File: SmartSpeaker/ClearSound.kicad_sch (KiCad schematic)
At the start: 51 parts

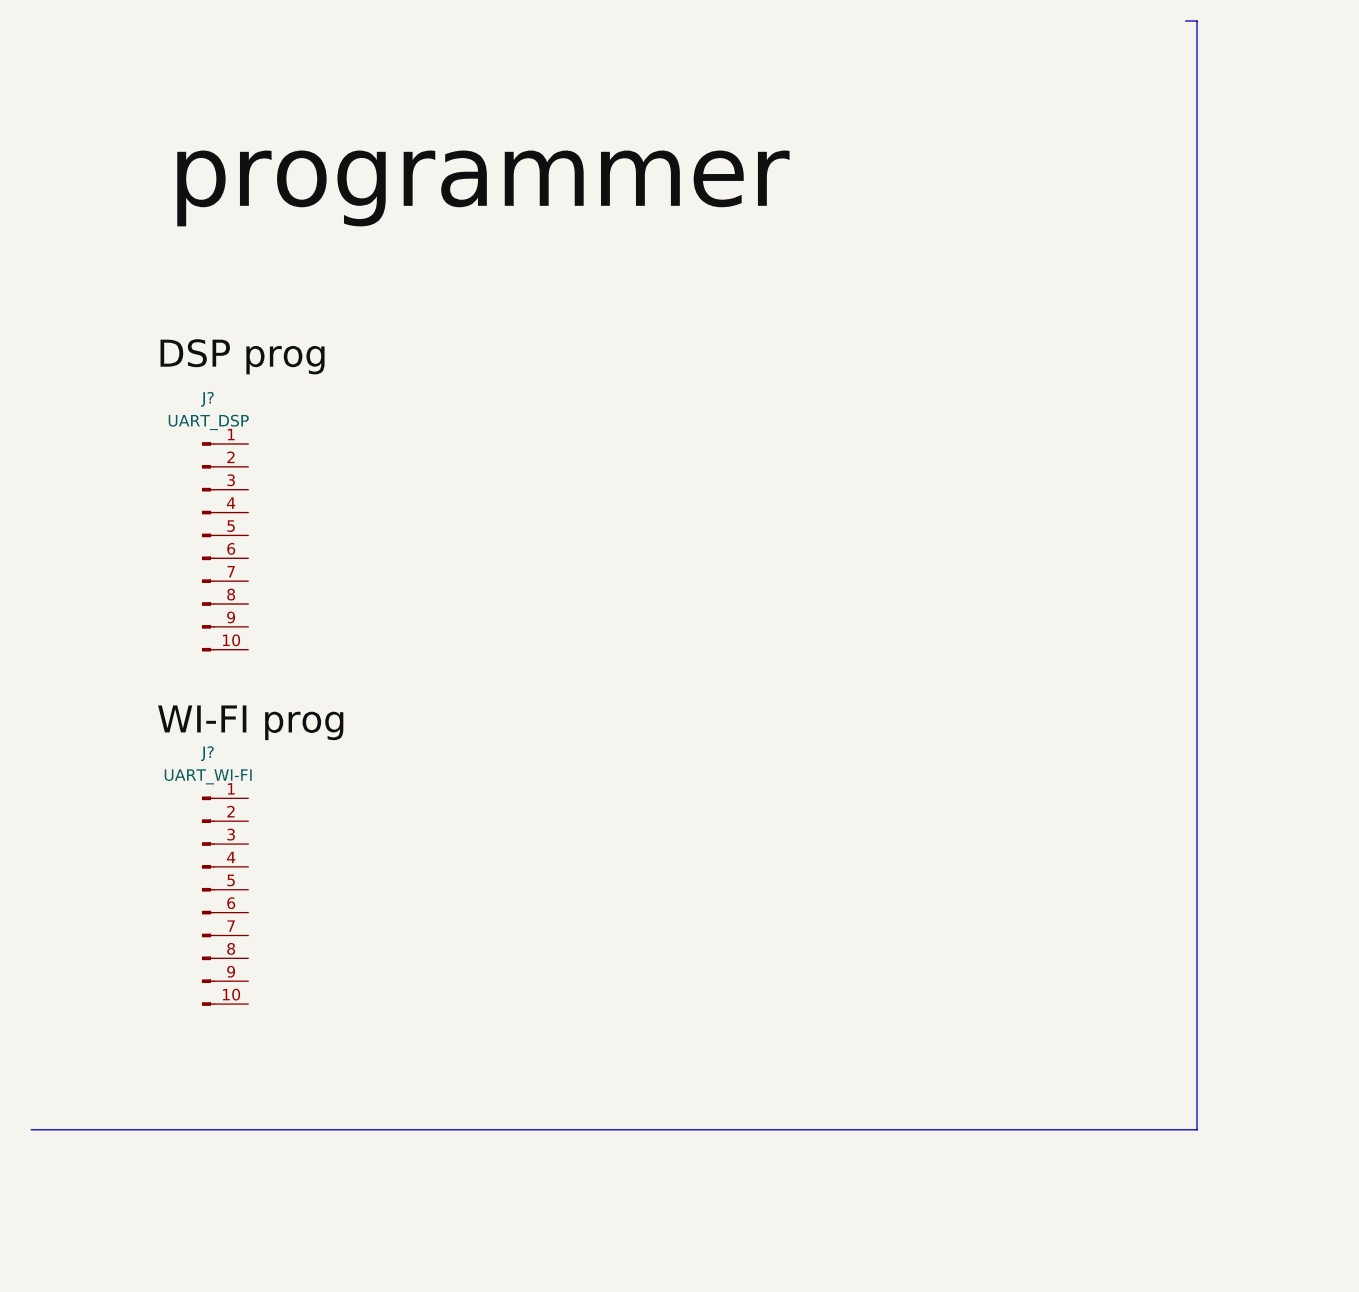
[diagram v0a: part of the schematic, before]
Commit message: UART header VDD/GND and interconnect now actually saved
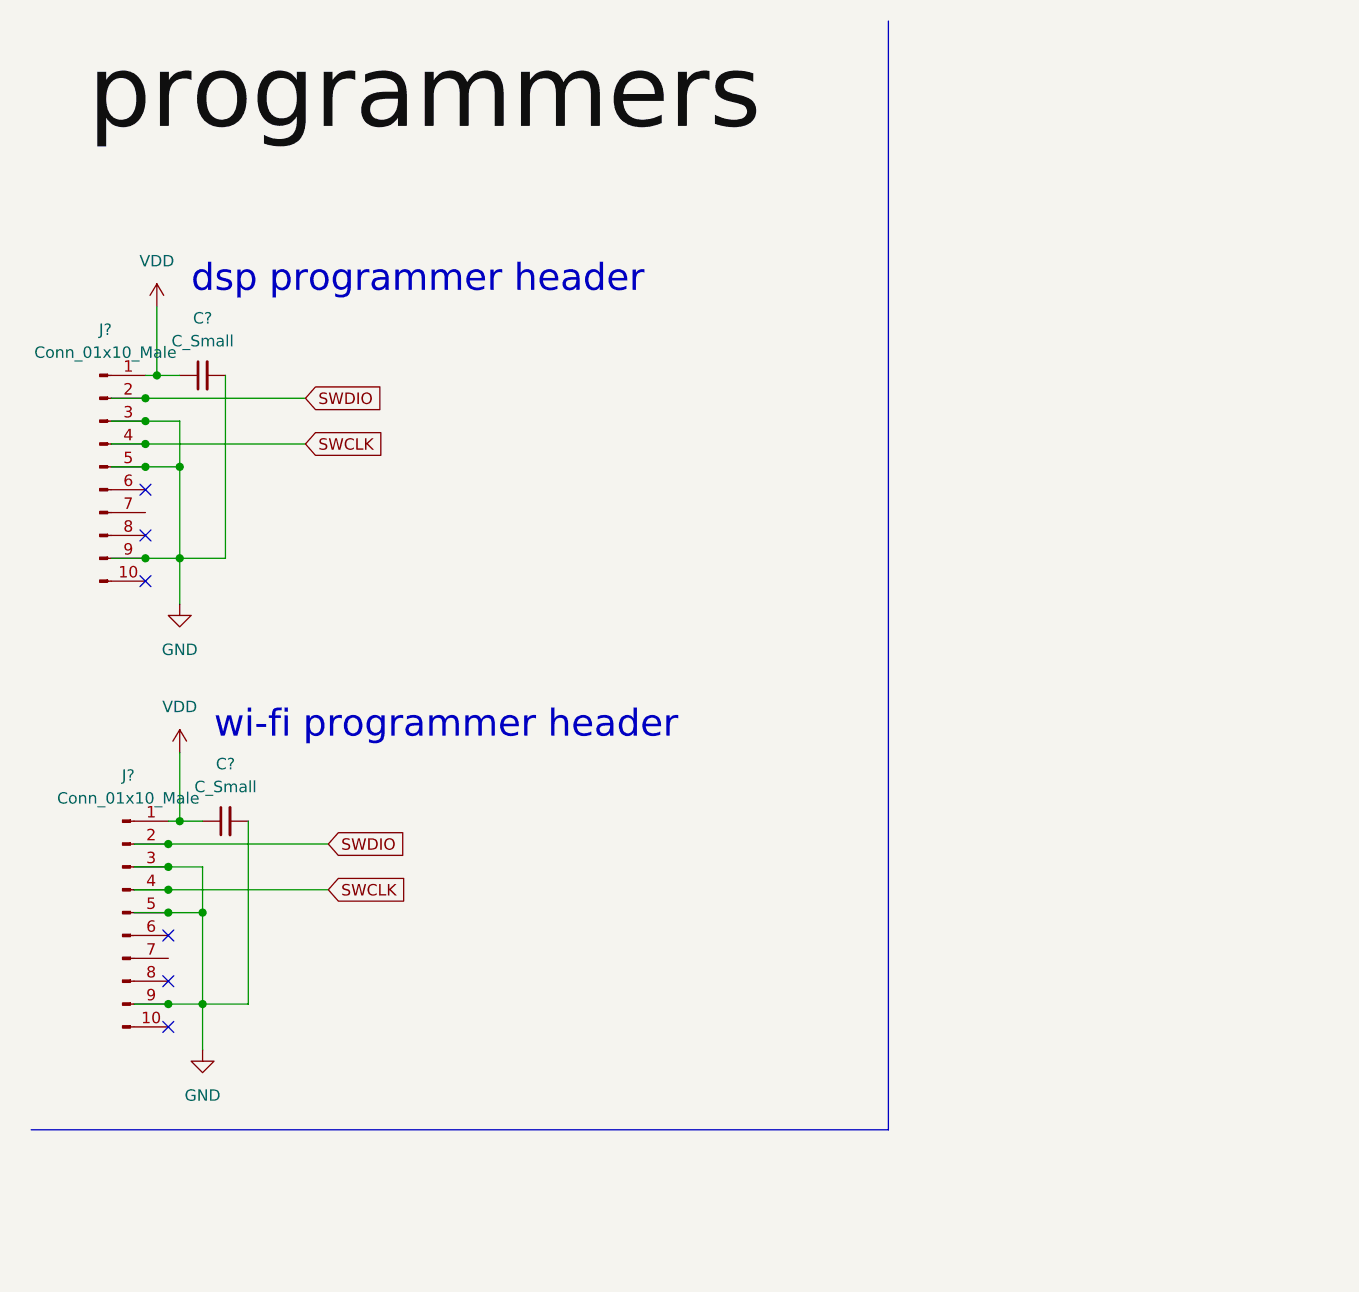
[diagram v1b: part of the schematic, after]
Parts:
- removed J?: UART_DSP, symbol Connector:Conn_01x10_Male
- removed J?: UART_WI-FI, symbol Connector:Conn_01x10_Male
- added C? (x2): C_Small, Capacitor_SMD:C_0402_1005Metric, symbol Device:C_Small
- added J? (x2): Conn_01x10_Male, Connector_PinHeader_1.27mm:PinHeader_1x10_P1.27mm_Vertical, symbol Connector:Conn_01x10_Male
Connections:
- net GND: now also C?.2, C?.2, J?.3 (Pin_3), J?.3 (Pin_3), J?.5 (Pin_5), J?.5 (Pin_5), J?.9 (Pin_9), J?.9 (Pin_9)
- net VDD: now also C?.1, C?.1, J?.1 (Pin_1), J?.1 (Pin_1)
- new net SWCLK: J?.4 (Pin_4), J?.4 (Pin_4)
- new net SWDIO: J?.2 (Pin_2), J?.2 (Pin_2)
- no-connect marks 0 -> 6
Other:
- note added: "dsp programmer header"
- note added: "wi-fi programmer header"

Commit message: change programmer header to use smaller footprint
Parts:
- removed C? (x2): C_Small, Capacitor_SMD:C_0402_1005Metric, symbol Device:C_Small
- removed J? (x2): Conn_01x10_Male, Connector_PinHeader_1.27mm:PinHeader_1x10_P1.27mm_Vertical, symbol Connector:Conn_01x10_Male
- added JP1, JP2: (no value), symbol Connector:Conn_01x04_Male
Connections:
- net DSP UART RX: now also IC?.K4 (UART0_TX); no longer IC?.K3 (UART0_RX)
- net DSP UART TX: now also IC?.K3 (UART0_RX); no longer IC?.K4 (UART0_TX)
- net GND: now also JP1.2 (Pin_2), JP2.2 (Pin_2)
- net VDD: now also JP1.1 (Pin_1), JP2.1 (Pin_1)
- net WIFI UART RX: now also IC?.L9 (UART_TXD), JP1.4 (Pin_4), JP2.4 (Pin_4); no longer IC?.M10 (UART_RXD)
- net WIFI UART TX: now also IC?.M10 (UART_RXD), JP1.3 (Pin_3), JP2.3 (Pin_3); no longer IC?.L9 (UART_TXD)
- no-connect marks 6 -> 0
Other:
- note removed: "dsp programmer header"
- note removed: "wi-fi programmer header"

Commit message: add UART flow control
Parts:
- removed JP1, JP2: (no value), symbol Connector:Conn_01x04_Male
- added JP1, JP2: (no value), symbol Connector:Conn_01x06_Male
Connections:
- net DSP UART RX: now also JP1.4 (Pin_4)
- net DSP UART TX: now also JP1.3 (Pin_3)
- net GND: now also JP1.2 (Pin_2), JP2.2 (Pin_2)
- net I2S_BCLK: now also IC?.L1 (I2S0_BCLK)
- net VDD: now also JP1.1 (Pin_1), JP2.1 (Pin_1)
- net WIFI UART RX: now also JP2.4 (Pin_4)
- net WIFI UART TX: now also JP2.3 (Pin_3)
- net WIFI UART RTS: now reaches IC?.K10 (GPIOC8)
- net WIFI UART RTS: now also IC?.L3 (UART0_CTS), JP2.5 (Pin_5)
- net WIFI UART CTS: now reaches IC?.K12 (GPIOC7)
- net WIFI UART CTS: now also IC?.L4 (UART0_RTS), JP2.6 (Pin_6)
- new net DSP UART CTS: JP1.6 (Pin_6)
- new net DSP UART RTS: JP1.5 (Pin_5)

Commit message: add I2C to dsp chip
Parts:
- added R?: (no value), symbol Device:R_Small
- added R?: R_Small, symbol Device:R_Small
- JP1: value (none) -> UART dsp
- JP2: value (none) -> UART wi-fi
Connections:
- net VDD: now also R?.1, R?.2
- net I2C clock line: now reaches IC?.C7 (I2C0_SCL)
- net I2C clock line: now also R?.1
- net I2C data line: now reaches IC?.D8 (I2C0_SDA)
- net I2C data line: now also R?.2
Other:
- moved on the sheet: IC?

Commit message: added antenna footprint
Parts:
- added E?: (no value), symbol YC0009AA:YC0009AA
- R?: value (none) -> R_Small
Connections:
- net GND: now also E?.2, E?.3
- net ANTENNA: no longer names the net of IC?.A11 (ANT)
- net ANTENNA: now also E?.1
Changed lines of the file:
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@@
     (stroke (width 0) (type default) (color 0 0 0 0))
   )
+  (wire (pts (xy 26.67 521.97) (xy 24.13 521.97))
+    (stroke (width 0) (type default) (color 0 0 0 0))
+  )
   (wire (pts (xy 398.78 35.56) (xy 398.78 38.1))
     (stroke (width 0) (type default) (color 0 0 0 0))
@@
     (stroke (width 0) (type default) (color 0 0 0 0))
   )
+  (wire (pts (xy 24.13 521.97) (xy 24.13 530.86))
+    (stroke (width 0) (type default) (color 0 0 0 0))
+  )
   (wire (pts (xy 491.49 134.62) (xy 491.49 139.7))
     (stroke (width 0) (type default) (color 0 0 0 0))
@@
     (stroke (width 0) (type default) (color 0 0 0 0))
   )
-  (wire (pts (xy 50.8 557.53) (xy 64.77 557.53))
+  (wire (pts (xy 19.05 557.53) (xy 64.77 557.53))
     (stroke (width 0) (type default) (color 0 0 0 0))
   )
@@
     (stroke (width 0) (type default) (color 0 0 0 0))
   )
+  (wire (pts (xy 19.05 557.53) (xy 19.05 519.43))
+    (stroke (width 0) (type default) (color 0 0 0 0))
+  )
   (wire (pts (xy 483.87 242.57) (xy 492.76 242.57))
     (stroke (width 0) (type default) (color 0 0 0 0))
@@
     (stroke (width 0) (type default) (color 0 0 0 0))
   )
+  (wire (pts (xy 19.05 519.43) (xy 26.67 519.43))
+    (stroke (width 0) (type default) (color 0 0 0 0))
+  )
   (wire (pts (xy 532.13 337.82) (xy 543.56 337.82))
     (stroke (width 0) (type default) (color 0 0 0 0))
@@
     )
   )
-  (global_label "ANTENNA" (shape input) (at 50.8 557.53 180) (fields_autoplaced)
-    (effects (font (size 1.27 1.27)) (justify right))
-    (property "Intersheet References" "${INTERSHEET_REFS}" (id 0) (at 40.1017 557.4506 0)
-      (effects (font (size 1.27 1.27)) (justify right) hide)
-    )
-  )
   (global_label "I2C clock line" (shape input) (at 237.49 288.29 180) (fields_autoplaced)
     (effects (font (size 1.27 1.27)) (justify right))
@@
       (effects (font (size 1.27 1.27)) hide)
     )
-    (property "Value" "" (id 1) (at 218.44 313.6899 90)
+    (property "Value" "VDD" (id 1) (at 218.44 313.6899 90)
       (effects (font (size 1.27 1.27)) (justify left))
     )
@@
     (pin "1")
   )
+  (symbol (lib_id "power:GND") (at 24.13 530.86 0) (unit 1)
+    (in_bom yes) (on_board yes) (fields_autoplaced)
+    (property "Reference" "#PWR?" (id 0) (at 24.13 537.21 0)
+      (effects (font (size 1.27 1.27)) hide)
+    )
+    (property "Value" "" (id 1) (at 24.13 535.94 0))
+    (property "Footprint" "" (id 2) (at 24.13 530.86 0)
+      (effects (font (size 1.27 1.27)) hide)
+    )
+    (property "Datasheet" "" (id 3) (at 24.13 530.86 0)
+      (effects (font (size 1.27 1.27)) hide)
+    )
+    (pin "1")
+  )
   (symbol (lib_id "AMP:TPA3138D2PWPR") (at 443.23 234.95 0) (unit 1)
     (in_bom yes) (on_board yes) (fields_autoplaced)
@@
       (effects (font (size 1.27 1.27)) (justify left))
     )
-    (property "Value" "" (id 1) (at 242.57 304.7999 0)
+    (property "Value" "R_Small" (id 1) (at 242.57 304.7999 0)
       (effects (font (size 1.27 1.27)) (justify left))
     )
@@
     (pin "1")
   )
+  (symbol (lib_id "YC0009AA:YC0009AA") (at 29.21 519.43 0) (unit 1)
+    (in_bom yes) (on_board yes) (fields_autoplaced)
+    (property "Reference" "E?" (id 0) (at 31.75 518.6044 0)
+      (effects (font (size 1.27 1.27)) (justify left))
+    )
+    (property "Value" "" (id 1) (at 31.75 521.1444 0)
+      (effects (font (size 1.27 1.27)) (justify left))
+    )
+    (property "Footprint" "" (id 2) (at 29.21 519.43 0)
+      (effects (font (size 1.27 1.27)) (justify left bottom) hide)
+    )
+    (property "Datasheet" "" (id 3) (at 29.21 519.43 0)
+      (effects (font (size 1.27 1.27)) (justify left bottom) hide)
+    )
+    (property "MANUFACTURER" "Quectel" (id 4) (at 29.21 519.43 0)
+      (effects (font (size 1.27 1.27)) (justify left bottom) hide)
+    )
+    (property "MAXIMUM_PACKAGE_HEIGHT" "0.6 mm" (id 5) (at 29.21 519.43 0)
+      (effects (font (size 1.27 1.27)) (justify left bottom) hide)
+    )
+    (property "PARTREV" "1.1" (id 6) (at 29.21 519.43 0)
+      (effects (font (size 1.27 1.27)) (justify left bottom) hide)
+    )
+    (property "STANDARD" "Manufacturer Recommendations" (id 7) (at 29.21 519.43 0)
+      (effects (font (size 1.27 1.27)) (justify left bottom) hide)
+    )
+    (pin "1")
+    (pin "2")
+    (pin "3")
+  )
   (symbol (lib_id "Device:C_Small") (at 431.8 90.17 0) (unit 1)
     (in_bom yes) (on_board yes)
@@
       (reference "#PWR?") (unit 1) (value "GND") (footprint "")
     )
+    (path "/3ce928af-6e41-4e1e-b2c7-efb295c51906"
+      (reference "#PWR?") (unit 1) (value "GND") (footprint "")
+    )
     (path "/4261c569-667c-4d80-a660-4f7983197f92"
       (reference "#PWR?") (unit 1) (value "GND") (footprint "")
@@
       (reference "C?") (unit 1) (value "1000pF") (footprint "")
     )
+    (path "/9611b1bf-2a0f-46d2-832e-858585f10d78"
+      (reference "E?") (unit 1) (value "YC0009AA") (footprint "XCVR_YC0009AA")
+    )
     (path "/0bff3beb-fb1b-41bb-9745-f5ce5c3e0e0f"

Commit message: I2C stuff on wifi
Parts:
- E?: value (none) -> YC0009AA; footprint (none) -> XCVR_YC0009AA
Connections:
- net I2C CLK line: now reaches IC?.E1 (GPIOA7)
- net I2S CLK line: now reaches IC?.F2 (GPIOA10)
- net I2S DATA line: now reaches IC?.F4 (GPIOA4)
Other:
- moved on the sheet: E?
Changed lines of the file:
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@@
     (stroke (width 0) (type default) (color 0 0 0 0))
   )
-  (wire (pts (xy 26.67 521.97) (xy 24.13 521.97))
+  (wire (pts (xy 33.02 521.97) (xy 30.48 521.97))
     (stroke (width 0) (type default) (color 0 0 0 0))
   )
@@
     (stroke (width 0) (type default) (color 0 0 0 0))
   )
-  (wire (pts (xy 24.13 521.97) (xy 24.13 530.86))
+  (wire (pts (xy 30.48 521.97) (xy 30.48 530.86))
     (stroke (width 0) (type default) (color 0 0 0 0))
   )
@@
     (stroke (width 0) (type default) (color 0 0 0 0))
   )
-  (wire (pts (xy 19.05 557.53) (xy 64.77 557.53))
+  (wire (pts (xy 25.4 557.53) (xy 64.77 557.53))
     (stroke (width 0) (type default) (color 0 0 0 0))
   )
@@
     (stroke (width 0) (type default) (color 0 0 0 0))
   )
-  (wire (pts (xy 19.05 557.53) (xy 19.05 519.43))
+  (wire (pts (xy 25.4 557.53) (xy 25.4 519.43))
     (stroke (width 0) (type default) (color 0 0 0 0))
   )
@@
     (stroke (width 0) (type default) (color 0 0 0 0))
   )
-  (wire (pts (xy 19.05 519.43) (xy 26.67 519.43))
+  (wire (pts (xy 25.4 519.43) (xy 33.02 519.43))
     (stroke (width 0) (type default) (color 0 0 0 0))
   )
@@
     (stroke (width 0) (type default) (color 0 0 0 0))
   )
+  (wire (pts (xy 50.8 623.57) (xy 64.77 623.57))
+    (stroke (width 0) (type default) (color 0 0 0 0))
+  )
   (wire (pts (xy 412.75 238.76) (xy 412.75 222.25))
     (stroke (width 0) (type default) (color 0 0 0 0))
@@
     (stroke (width 0) (type default) (color 0 0 0 0))
   )
+  (wire (pts (xy 50.8 605.79) (xy 64.77 605.79))
+    (stroke (width 0) (type default) (color 0 0 0 0))
+  )
   (wire (pts (xy 420.37 50.8) (xy 420.37 53.34))
     (stroke (width 0) (type default) (color 0 0 0 0))
@@
   )
   (wire (pts (xy 416.56 234.95) (xy 416.56 237.49))
+    (stroke (width 0) (type default) (color 0 0 0 0))
+  )
+  (wire (pts (xy 50.8 621.03) (xy 64.77 621.03))
     (stroke (width 0) (type default) (color 0 0 0 0))
   )
@@
     )
   )
+  (global_label "I2S DATA line" (shape input) (at 50.8 623.57 180) (fields_autoplaced)
+    (effects (font (size 1.27 1.27)) (justify right))
+    (property "Intersheet References" "${INTERSHEET_REFS}" (id 0) (at 35.5055 623.4906 0)
+      (effects (font (size 1.27 1.27)) (justify right) hide)
+    )
+  )
   (global_label "I2C clock line" (shape input) (at 237.49 288.29 180) (fields_autoplaced)
     (effects (font (size 1.27 1.27)) (justify right))
@@
     )
   )
+  (global_label "I2C CLK line" (shape input) (at 50.8 605.79 180) (fields_autoplaced)
+    (effects (font (size 1.27 1.27)) (justify right))
+    (property "Intersheet References" "${INTERSHEET_REFS}" (id 0) (at 36.2917 605.7106 0)
+      (effects (font (size 1.27 1.27)) (justify right) hide)
+    )
+  )
   (global_label "WIFI UART CTS" (shape input) (at 44.45 97.79 0) (fields_autoplaced)
     (effects (font (size 1.27 1.27)) (justify left))
@@
     (property "Intersheet References" "${INTERSHEET_REFS}" (id 0) (at 59.6841 53.2606 0)
       (effects (font (size 1.27 1.27)) (justify left) hide)
+    )
+  )
+  (global_label "I2S CLK line" (shape input) (at 50.8 621.03 180) (fields_autoplaced)
+    (effects (font (size 1.27 1.27)) (justify right))
+    (property "Intersheet References" "${INTERSHEET_REFS}" (id 0) (at 36.3521 620.9506 0)
+      (effects (font (size 1.27 1.27)) (justify right) hide)
     )
   )
@@
     (pin "1")
   )
-  (symbol (lib_id "power:GND") (at 24.13 530.86 0) (unit 1)
-    (in_bom yes) (on_board yes) (fields_autoplaced)
-    (property "Reference" "#PWR?" (id 0) (at 24.13 537.21 0)
-      (effects (font (size 1.27 1.27)) hide)
-    )
-    (property "Value" "" (id 1) (at 24.13 535.94 0))
-    (property "Footprint" "" (id 2) (at 24.13 530.86 0)
-      (effects (font (size 1.27 1.27)) hide)
-    )
-    (property "Datasheet" "" (id 3) (at 24.13 530.86 0)
+  (symbol (lib_id "power:GND") (at 30.48 530.86 0) (unit 1)
+    (in_bom yes) (on_board yes) (fields_autoplaced)
+    (property "Reference" "#PWR?" (id 0) (at 30.48 537.21 0)
+      (effects (font (size 1.27 1.27)) hide)
+    )
+    (property "Value" "GND" (id 1) (at 30.48 535.94 0))
+    (property "Footprint" "" (id 2) (at 30.48 530.86 0)
+      (effects (font (size 1.27 1.27)) hide)
+    )
+    (property "Datasheet" "" (id 3) (at 30.48 530.86 0)
       (effects (font (size 1.27 1.27)) hide)
     )
@@
     (pin "1")
   )
-  (symbol (lib_id "YC0009AA:YC0009AA") (at 29.21 519.43 0) (unit 1)
-    (in_bom yes) (on_board yes) (fields_autoplaced)
-    (property "Reference" "E?" (id 0) (at 31.75 518.6044 0)
-      (effects (font (size 1.27 1.27)) (justify left))
-    )
-    (property "Value" "" (id 1) (at 31.75 521.1444 0)
-      (effects (font (size 1.27 1.27)) (justify left))
-    )
-    (property "Footprint" "" (id 2) (at 29.21 519.43 0)
+  (symbol (lib_id "YC0009AA:YC0009AA") (at 35.56 519.43 0) (unit 1)
+    (in_bom yes) (on_board yes) (fields_autoplaced)
+    (property "Reference" "E?" (id 0) (at 38.1 518.6044 0)
+      (effects (font (size 1.27 1.27)) (justify left))
+    )
+    (property "Value" "YC0009AA" (id 1) (at 38.1 521.1444 0)
+      (effects (font (size 1.27 1.27)) (justify left))
+    )
+    (property "Footprint" "XCVR_YC0009AA" (id 2) (at 35.56 519.43 0)
       (effects (font (size 1.27 1.27)) (justify left bottom) hide)
     )
-    (property "Datasheet" "" (id 3) (at 29.21 519.43 0)
+    (property "Datasheet" "" (id 3) (at 35.56 519.43 0)
       (effects (font (size 1.27 1.27)) (justify left bottom) hide)
     )
-    (property "MANUFACTURER" "Quectel" (id 4) (at 29.21 519.43 0)
+    (property "MANUFACTURER" "Quectel" (id 4) (at 35.56 519.43 0)
       (effects (font (size 1.27 1.27)) (justify left bottom) hide)
     )
-    (property "MAXIMUM_PACKAGE_HEIGHT" "0.6 mm" (id 5) (at 29.21 519.43 0)
+    (property "MAXIMUM_PACKAGE_HEIGHT" "0.6 mm" (id 5) (at 35.56 519.43 0)
       (effects (font (size 1.27 1.27)) (justify left bottom) hide)
     )
-    (property "PARTREV" "1.1" (id 6) (at 29.21 519.43 0)
+    (property "PARTREV" "1.1" (id 6) (at 35.56 519.43 0)
       (effects (font (size 1.27 1.27)) (justify left bottom) hide)
     )
-    (property "STANDARD" "Manufacturer Recommendations" (id 7) (at 29.21 519.43 0)
+    (property "STANDARD" "Manufacturer Recommendations" (id 7) (at 35.56 519.43 0)
       (effects (font (size 1.27 1.27)) (justify left bottom) hide)
     )

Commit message: add power button
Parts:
- added C?: C_Small, Capacitor_SMD:C_0402_1005Metric, symbol Device:C_Small
- added D?: LED_Small_Filled, LED_SMD:LED_0805_2012Metric, symbol Device:LED_Small_Filled
- added R?: 2.2k, Resistor_SMD:R_01005_0402Metric, symbol Device:R_Small
- added R?: 100k, Resistor_SMD:R_01005_0402Metric, symbol Device:R_Small
- added R?: 100, Resistor_SMD:R_01005_0402Metric, symbol Device:R_Small
- added SW?: SW_Push_Dual, Button_Switch_SMD:SW_MEC_5GSH9, symbol Switch:SW_Push_Dual
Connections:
- net GND: now also C?.2, SW?.2, SW?.4
- net VDD: now also R?.1, R?.1
- net POWER BUTTON: now reaches IC?.B15 (M3_PWREN)
- net POWER BUTTON: now also C?.1, D?.1 (K), R?.1, R?.2
- new net: D?.2 (A), R?.2
- new net: R?.2, SW?.1, SW?.3
